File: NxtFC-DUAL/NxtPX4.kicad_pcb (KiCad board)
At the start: 4 copper layers, 33 x 27 mm, 137 parts, among them J1 USB_C_Receptacle_USB2.0, J10 Micro_SD_Card, J11 Debug, J12 AuxGPIO, J2 DJIO3, J3 GPS, J4 UART2, J5 Upper computer connector, J6 ESC, J7 Upper computer connector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

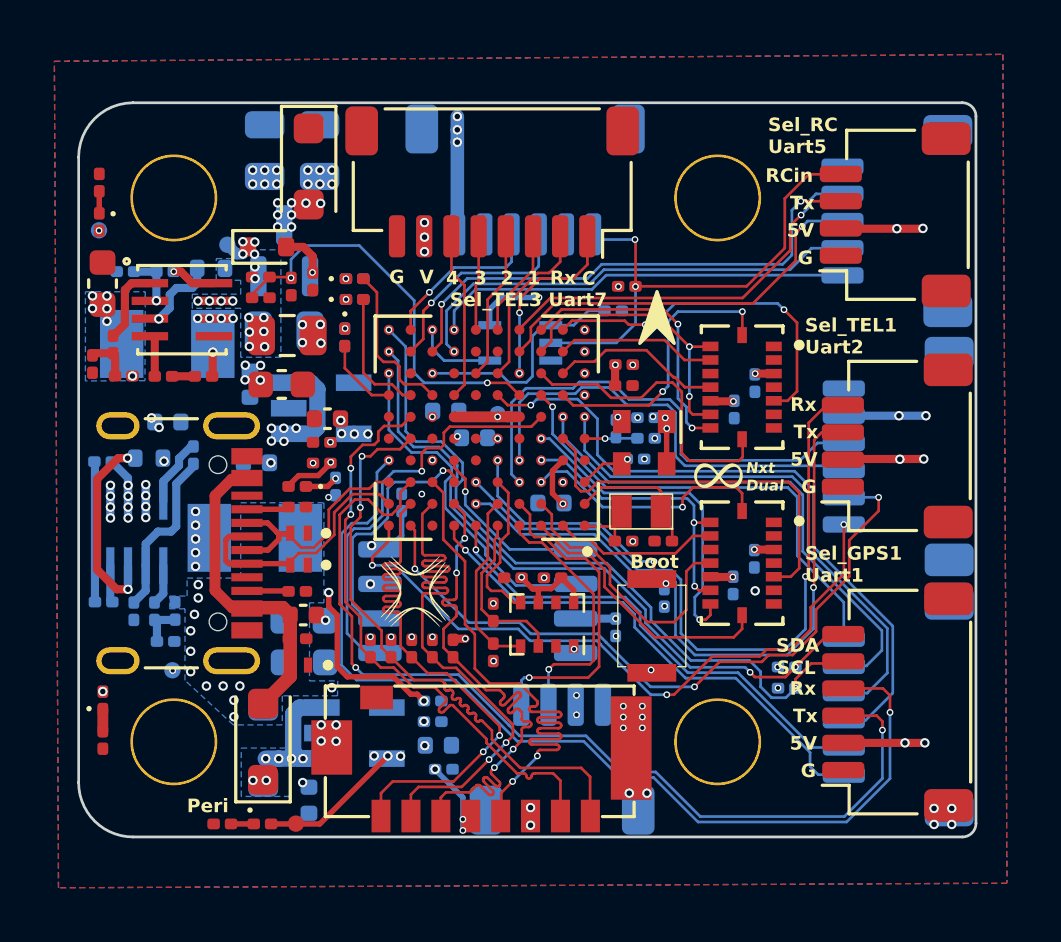
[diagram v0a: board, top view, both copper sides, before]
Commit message: [Rlease][Dual]: Update logo for Dual version
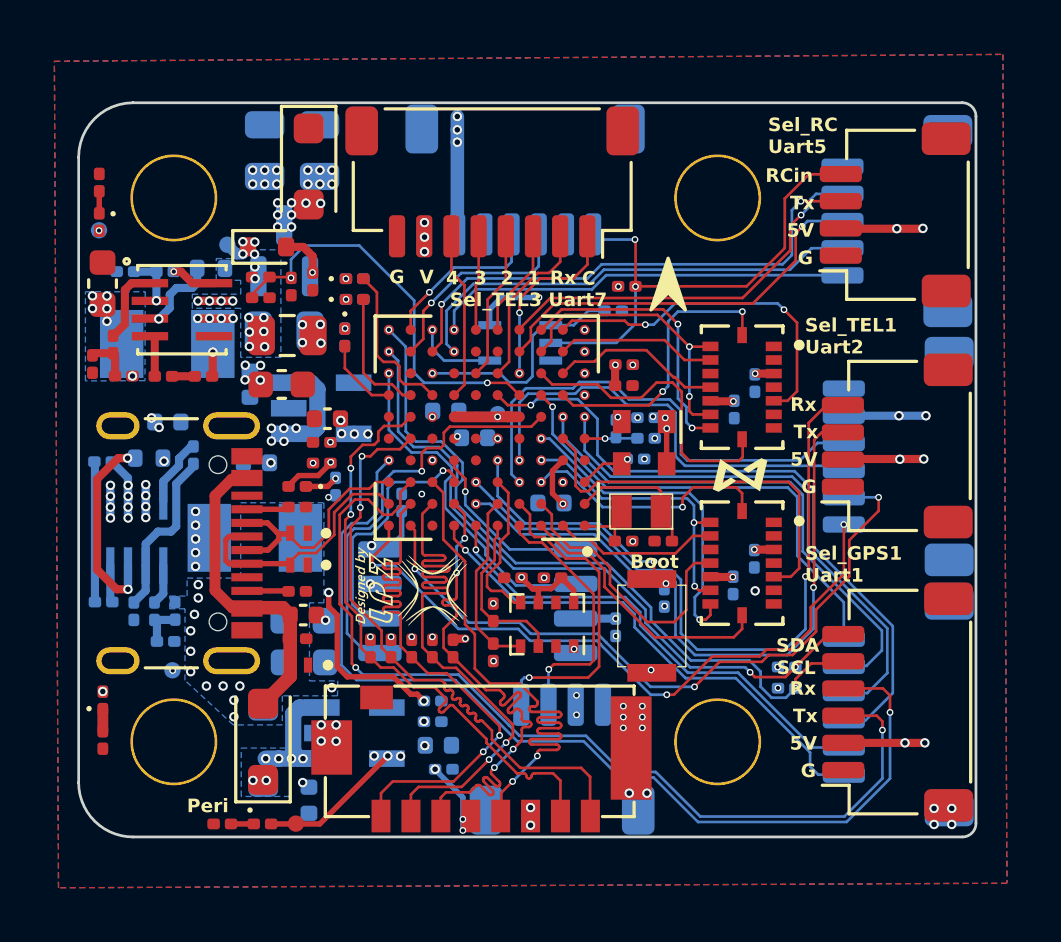
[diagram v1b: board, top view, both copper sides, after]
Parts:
- removed U17: UAV_LOGO, NxtPX4:Dual_logo
- added U7: NxtLOGO, NxtPX4:NxtLOGO, F.Cu at (114.3, 73.0)
- U8: moved to F.Cu
- moved U8 8.59 mm to (100.9, 77.8), turned to 90 degrees
- moved U6 1.30 mm to (111.7, 67.0)
- moved U5 0.64 mm to (102.9, 77.9)
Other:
- board text removed: "Nxt Dual"
